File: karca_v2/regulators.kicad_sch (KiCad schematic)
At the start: 30 parts, among them J1 CON_FAN1, J2 Conn_Batt, J3 USB_B_Micro, Q1 AO3401A, SW1 SW_SPST, SW2 SW_SPST, SW3 SW_SPST, U1 TVS1400DRV

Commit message: updated POS
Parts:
- F1: now not fitted; now left out of the parts list
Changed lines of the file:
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@@
 		(unit 1)
 		(exclude_from_sim no)
-		(in_bom yes)
+		(in_bom no)
 		(on_board yes)
-		(dnp no)
+		(dnp yes)
 		(fields_autoplaced yes)
 		(property "Reference" "F1"

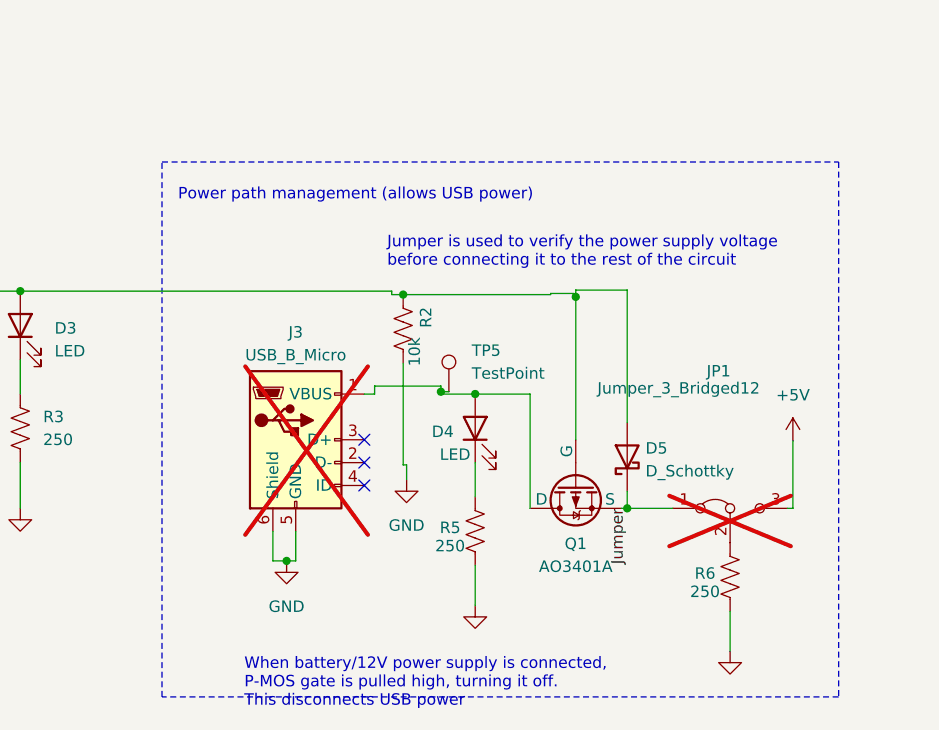
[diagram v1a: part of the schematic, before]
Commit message: Replaced header with a smaller one, added silksreen labels, and removed secondary USB power source
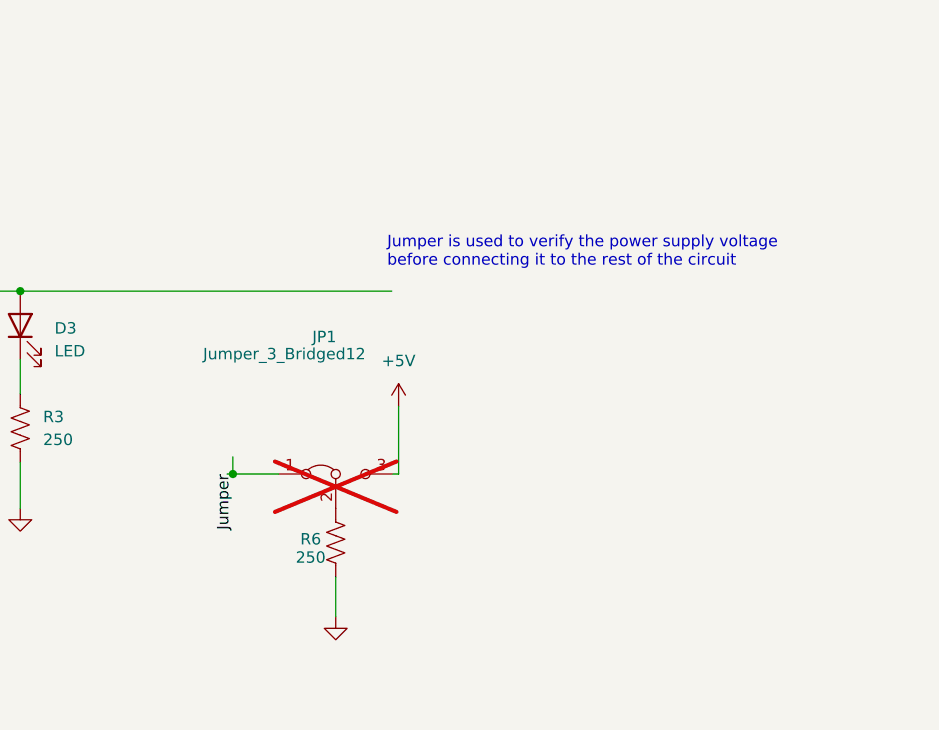
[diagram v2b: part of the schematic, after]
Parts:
- removed D4: LED, LED_SMD:LED_1206_3216Metric, symbol Device:LED
- removed D5: D_Schottky, Diode_SMD:D_SMA, symbol Device:D_Schottky
- removed J3: USB_B_Micro, custom-footprints:USB_Micro-B_Molex-105017-0001, symbol Connector:USB_B_Micro
- removed Q1: AO3401A, custom-footprints:SOT23-3, symbol Simulation_SPICE:PMOS
- removed R2: 10k, Resistor_SMD:R_1206_3216Metric, symbol Device:R_US
- removed R5: 250, Resistor_SMD:R_1206_3216Metric, symbol Device:R_US
- removed TP5: TestPoint, TestPoint:TestPoint_Pad_D2.0mm, symbol Connector:TestPoint
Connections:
- no-connect marks 10 -> 7
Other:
- note removed: "Power path management (allows USB power)"
- note removed: "When battery/12V power supply is connected, P-MOS gate is pulled high, turning it off. This disconnects USB power"
- moved on the sheet: JP1, R6

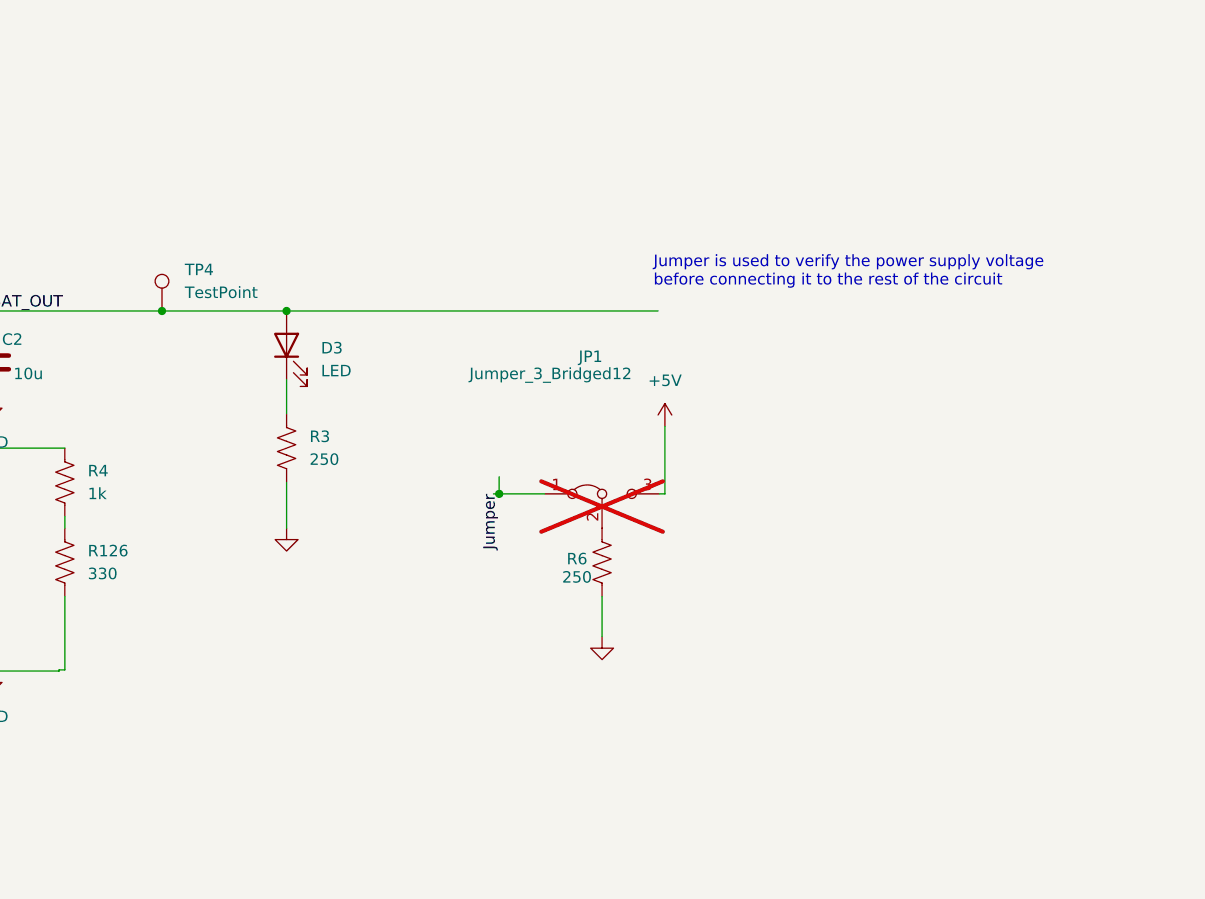
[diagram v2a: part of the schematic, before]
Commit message: changed pin header to a smaller one and removed USB secondary power supply
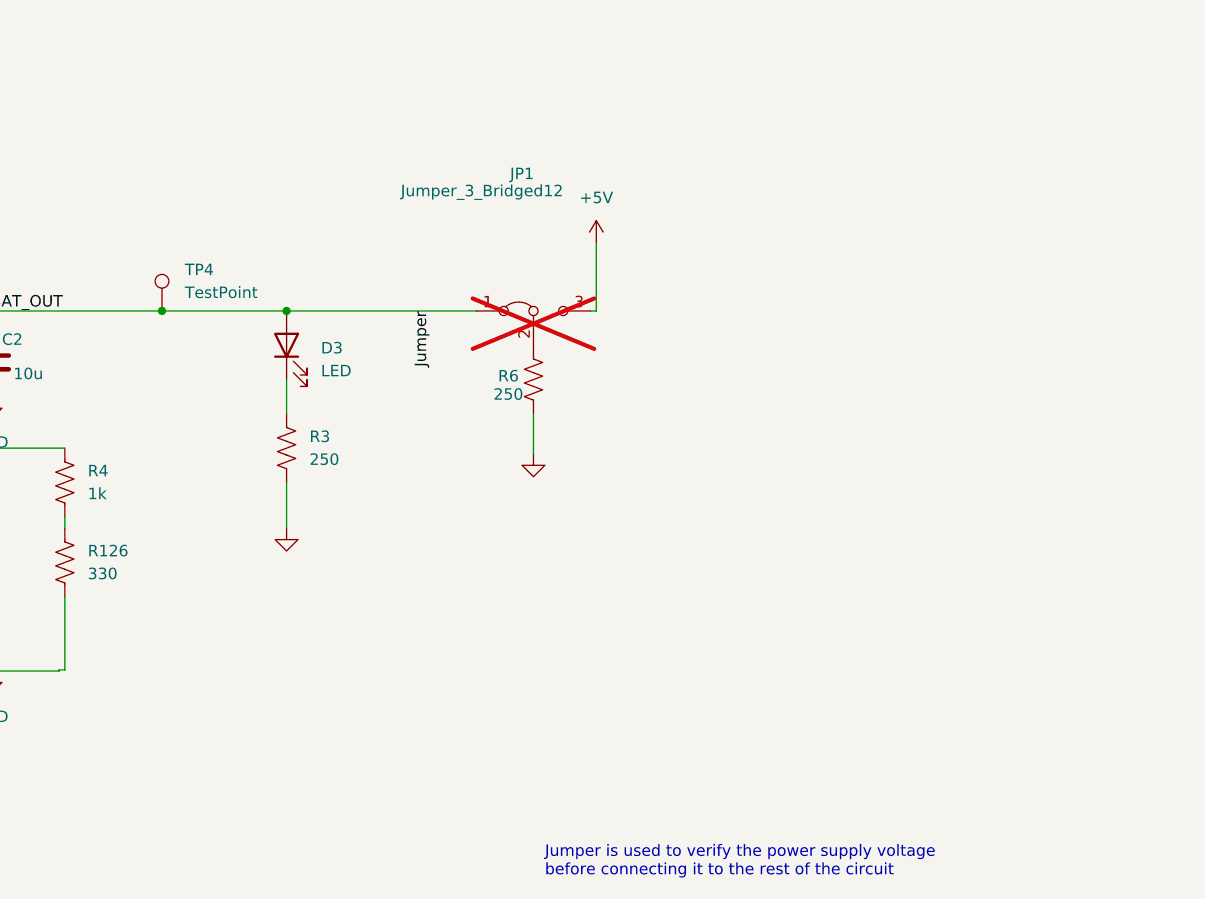
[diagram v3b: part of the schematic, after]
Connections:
- net Jumper is gone; now on net BAT_OUT: JP1.1 (A)
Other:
- moved on the sheet: JP1, R6
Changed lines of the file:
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@@
 	(text "Jumper is used to verify the power supply voltage\nbefore connecting it to the rest of the circuit"
 		(exclude_from_sim no)
-		(at 352.425 109.22 0)
+		(at 340.36 174.752 0)
 		(effects
 			(font
@@
 	)
 	(junction
-		(at 335.28 132.08)
+		(at 278.511 134.62)
 		(diameter 0)
 		(color 0 0 0 0)
 	)
 	(junction
-		(at 278.511 134.62)
+		(at 297.815 111.76)
 		(diameter 0)
 		(color 0 0 0 0)
 	)
 	(junction
-		(at 297.815 111.76)
+		(at 311.658 111.76)
 		(diameter 0)
 		(color 0 0 0 0)
@@
 		(color 0 0 0 0)
 	)
-	(junction
-		(at 311.658 111.76)
-		(diameter 0)
-		(color 0 0 0 0)
-	)
 	(no_connect
 		(at 214.63 116.84)
@@
 	(wire
 		(pts
-			(xy 353.06 132.08) (xy 353.695 132.08)
+			(xy 345.44 111.76) (xy 346.075 111.76)
 		)
 		(stroke
@@
 	(wire
 		(pts
-			(xy 311.658 111.76) (xy 297.815 111.76)
+			(xy 297.815 111.76) (xy 311.658 111.76)
 		)
 		(stroke
@@
 	(wire
 		(pts
-			(xy 335.28 132.08) (xy 335.28 130.175)
-		)
-		(stroke
-			(width 0)
-			(type default)
-		)
-	)
-	(wire
-		(pts
-			(xy 352.933 111.76) (xy 311.658 111.76)
-		)
-		(stroke
-			(width 0)
-			(type default)
-		)
-	)
-	(wire
-		(pts
 			(xy 21.463 84.709) (xy 30.353 84.709)
 		)
@@
 	(wire
 		(pts
-			(xy 353.695 124.587) (xy 353.695 132.08)
+			(xy 346.075 104.267) (xy 346.075 111.76)
 		)
 		(stroke
@@
 	(wire
 		(pts
-			(xy 335.28 132.08) (xy 340.36 132.08)
+			(xy 311.658 111.76) (xy 332.74 111.76)
 		)
 		(stroke
@@
 	(wire
 		(pts
-			(xy 334.645 132.08) (xy 335.28 132.08)
-		)
-		(stroke
-			(width 0)
-			(type default)
-		)
-	)
-	(wire
-		(pts
 			(xy 140.843 53.721) (xy 140.843 56.261)
 		)
@@
 	(wire
 		(pts
-			(xy 346.71 143.51) (xy 346.71 147.955)
+			(xy 339.09 123.19) (xy 339.09 127.635)
 		)
 		(stroke
@@
 	)
 	(label "Jumper"
-		(at 335.28 132.08 270)
+		(at 327.66 111.76 270)
 		(effects
 			(font
@@
 	(symbol
 		(lib_id "Device:R_US")
-		(at 346.71 139.7 0)
+		(at 339.09 119.38 0)
 		(unit 1)
 		(exclude_from_sim no)
@@
 		(dnp no)
 		(property "Reference" "R6"
-			(at 342.773 139.319 0)
+			(at 335.153 118.999 0)
 			(effects
 				(font
@@
 		)
 		(property "Value" "250"
-			(at 342.265 141.351 0)
+			(at 334.645 121.031 0)
 			(effects
 				(font
@@
 		)
 		(property "Footprint" "Resistor_SMD:R_1206_3216Metric"
-			(at 347.726 139.954 90)
+			(at 340.106 119.634 90)
 			(effects
 				(font
@@
 		)
 		(property "Datasheet" "~"
-			(at 346.71 139.7 0)
+			(at 339.09 119.38 0)
 			(effects
 				(font
@@
 		)
 		(property "Description" ""
-			(at 346.71 139.7 0)
+			(at 339.09 119.38 0)
 			(effects
 				(font
@@
 	(symbol
 		(lib_id "power:GND")
-		(at 346.71 147.955 0)
+		(at 339.09 127.635 0)
 		(unit 1)
 		(exclude_from_sim no)
@@
 		(dnp no)
 		(property "Reference" "#PWR014"
-			(at 346.71 154.305 0)
+			(at 339.09 133.985 0)
 			(effects
 				(font
@@
 		)
 		(property "Value" "GND"
-			(at 346.71 161.925 0)
+			(at 339.09 141.605 0)
 			(effects
 				(font
@@
 		)
 		(property "Footprint" ""
-			(at 346.71 147.955 0)
+			(at 339.09 127.635 0)
 			(effects
 				(font
@@
 		)
 		(property "Datasheet" ""
-			(at 346.71 147.955 0)
+			(at 339.09 127.635 0)
 			(effects
 				(font
@@
 		)
 		(property "Description" ""
-			(at 346.71 147.955 0)
+			(at 339.09 127.635 0)
 			(effects
 				(font
@@
 	(symbol
 		(lib_id "power:+5V")
-		(at 353.695 124.587 0)
+		(at 346.075 104.267 0)
 		(unit 1)
 		(exclude_from_sim no)
@@
 		(fields_autoplaced yes)
 		(property "Reference" "#PWR08"
-			(at 353.695 128.397 0)
+			(at 346.075 108.077 0)
 			(effects
 				(font
@@
 		)
 		(property "Value" "+5V"
-			(at 353.695 119.507 0)
+			(at 346.075 99.187 0)
 			(effects
 				(font
@@
 		)
 		(property "Footprint" ""
-			(at 353.695 124.587 0)
+			(at 346.075 104.267 0)
 			(effects
 				(font
@@
 		)
 		(property "Datasheet" ""
-			(at 353.695 124.587 0)
+			(at 346.075 104.267 0)
 			(effects
 				(font
@@
 		)
 		(property "Description" ""
-			(at 353.695 124.587 0)
+			(at 346.075 104.267 0)
 			(effects
 				(font
@@
 	(symbol
 		(lib_id "Jumper:Jumper_3_Bridged12")
-		(at 346.71 132.08 0)
+		(at 339.09 111.76 0)
 		(unit 1)
 		(exclude_from_sim no)
@@
 		(dnp yes)
 		(property "Reference" "JP1"
-			(at 345.44 116.84 0)
+			(at 337.82 96.52 0)
 			(effects
 				(font
@@
 		)
 		(property "Value" "Jumper_3_Bridged12"
-			(at 340.995 118.745 0)
+			(at 333.375 98.425 0)
 			(effects
 				(font
@@
 		)
 		(property "Footprint" "Connector_PinSocket_2.54mm:PinSocket_1x03_P2.54mm_Vertical"
-			(at 346.71 132.08 0)
+			(at 339.09 111.76 0)
 			(effects
 				(font
@@
 		)
 		(property "Datasheet" "~"
-			(at 346.71 132.08 0)
+			(at 339.09 111.76 0)
 			(effects
 				(font
@@
 		)
 		(property "Description" ""
-			(at 346.71 132.08 0)
+			(at 339.09 111.76 0)
 			(effects
 				(font

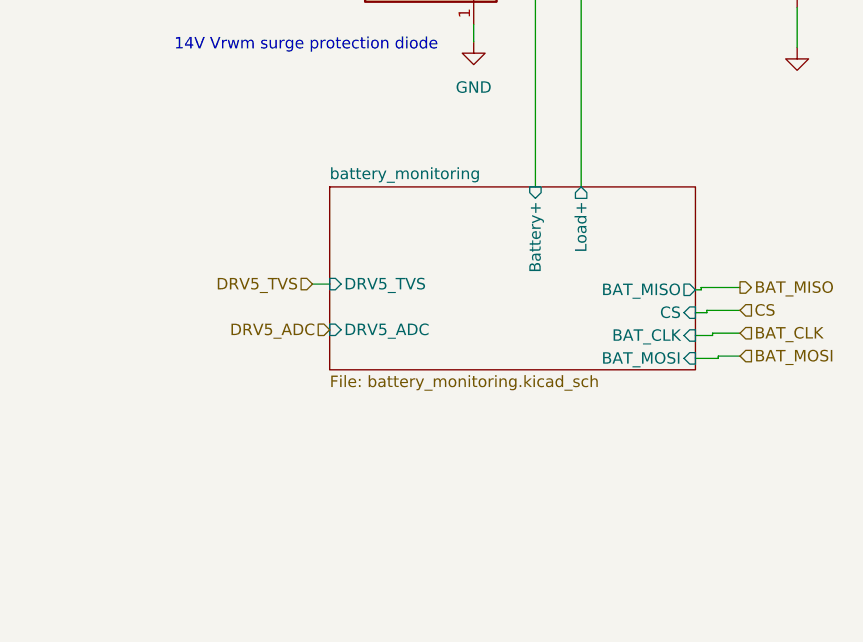
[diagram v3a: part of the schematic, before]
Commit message: reorganized ADCs
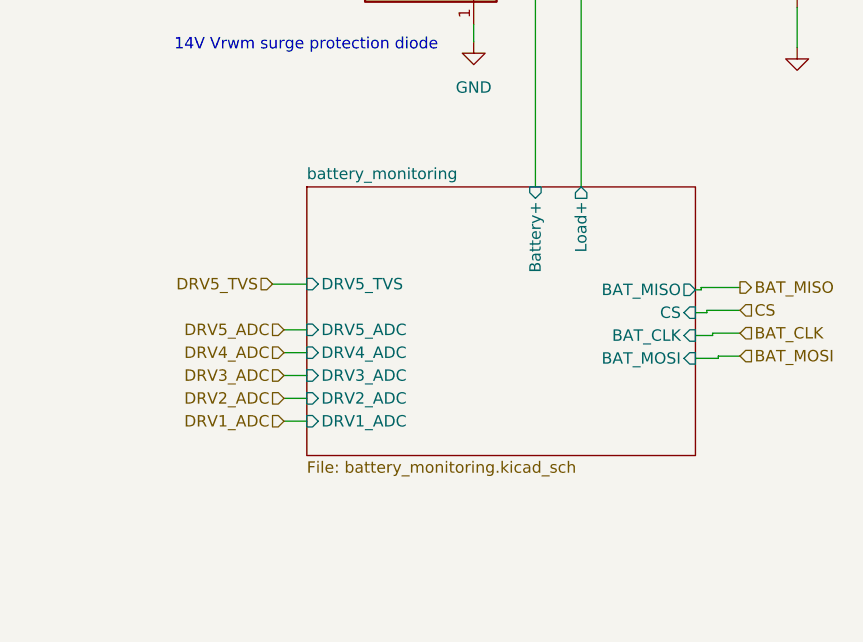
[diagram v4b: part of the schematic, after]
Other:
- sheet battery_monitoring ports: added DRV1_ADC, DRV2_ADC, DRV3_ADC, DRV4_ADC; removed none
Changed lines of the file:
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@@
 	(title_block
 		(title "kARCA 2.0 Engine Control System")
-		(date "2024-12-16")
-		(rev "1.1")
+		(date "2026-03-23")
+		(rev "1.2")
 		(company "Rice Eclipse")
 		(comment 1 "Designed by Deepak Narayan")
@@
 	(wire
 		(pts
+			(xy 46.99 134.62) (xy 49.53 134.62)
+		)
+		(stroke
+			(width 0)
+			(type default)
+		)
+	)
+	(wire
+		(pts
 			(xy 287.02 143.51) (xy 287.02 151.638)
 		)
@@
 	(wire
 		(pts
+			(xy 46.99 129.54) (xy 49.53 129.54)
+		)
+		(stroke
+			(width 0)
+			(type default)
+		)
+	)
+	(wire
+		(pts
 			(xy 275.59 111.76) (xy 278.765 111.76)
 		)
@@
 	(wire
 		(pts
+			(xy 46.99 139.7) (xy 49.53 139.7)
+		)
+		(stroke
+			(width 0)
+			(type default)
+		)
+	)
+	(wire
+		(pts
+			(xy 46.99 137.16) (xy 49.53 137.16)
+		)
+		(stroke
+			(width 0)
+			(type default)
+		)
+	)
+	(wire
+		(pts
 			(xy 275.59 134.62) (xy 278.511 134.62)
 		)
@@
 	(wire
 		(pts
+			(xy 46.99 132.08) (xy 49.53 132.08)
+		)
+		(stroke
+			(width 0)
+			(type default)
+		)
+	)
+	(wire
+		(pts
 			(xy 104.013 93.726) (xy 104.013 98.171)
 		)
@@
 	(wire
 		(pts
-			(xy 50.165 124.46) (xy 52.07 124.46)
+			(xy 45.72 124.46) (xy 49.53 124.46)
 		)
 		(stroke
@@
 		)
 	)
+	(hierarchical_label "DRV3_ADC"
+		(shape input)
+		(at 46.99 134.62 180)
+		(effects
+			(font
+				(size 1.27 1.27)
+			)
+			(justify right)
+		)
+	)
+	(hierarchical_label "DRV4_ADC"
+		(shape input)
+		(at 46.99 132.08 180)
+		(effects
+			(font
+				(size 1.27 1.27)
+			)
+			(justify right)
+		)
+	)
 	(hierarchical_label "DRV5_ADC"
 		(shape input)
-		(at 52.07 129.54 180)
+		(at 46.99 129.54 180)
 		(effects
 			(font
@@
 	(hierarchical_label "DRV5_TVS"
 		(shape input)
-		(at 50.165 124.46 180)
+		(at 45.72 124.46 180)
+		(effects
+			(font
+				(size 1.27 1.27)
+			)
+			(justify right)
+		)
+	)
+	(hierarchical_label "DRV1_ADC"
+		(shape input)
+		(at 46.99 139.7 180)
+		(effects
+			(font
+				(size 1.27 1.27)
+			)
+			(justify right)
+		)
+	)
+	(hierarchical_label "DRV2_ADC"
+		(shape input)
+		(at 46.99 137.16 180)
 		(effects
 			(font
@@
 	)
 	(sheet
-		(at 52.07 113.665)
-		(size 40.64 20.32)
+		(at 49.53 113.665)
+		(size 43.18 29.845)
 		(exclude_from_sim no)
 		(in_bom yes)
@@
 		)
 		(property "Sheetname" "battery_monitoring"
-			(at 52.07 112.9534 0)
+			(at 49.53 112.9534 0)
 			(effects
 				(font
@@
 		)
 		(property "Sheetfile" "battery_monitoring.kicad_sch"
-			(at 52.07 134.5696 0)
+			(at 49.53 144.0946 0)
 			(effects
 				(font
@@
 		)
 		(pin "DRV5_TVS" input
-			(at 52.07 124.46 180)
+			(at 49.53 124.46 180)
 			(effects
 				(font
@@
 		)
 		(pin "DRV5_ADC" input
-			(at 52.07 129.54 180)
+			(at 49.53 129.54 180)
+			(effects
+				(font
+					(size 1.27 1.27)
+				)
+				(justify left)
+			)
+		)
+		(pin "DRV4_ADC" input
+			(at 49.53 132.08 180)
+			(effects
+				(font
+					(size 1.27 1.27)
+				)
+				(justify left)
+			)
+		)
+		(pin "DRV3_ADC" input
+			(at 49.53 134.62 180)
+			(effects
+				(font
+					(size 1.27 1.27)
+				)
+				(justify left)
+			)
+		)
+		(pin "DRV1_ADC" input
+			(at 49.53 139.7 180)
+			(effects
+				(font
+					(size 1.27 1.27)
+				)
+				(justify left)
+			)
+		)
+		(pin "DRV2_ADC" input
+			(at 49.53 137.16 180)
 			(effects
 				(font
